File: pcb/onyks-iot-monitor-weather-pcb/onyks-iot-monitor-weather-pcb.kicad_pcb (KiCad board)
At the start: 2 copper layers, 100 x 82 mm, 32 parts, among them J1 53398-0371, J10 Conn_01x02_Pin, J11 Conn_01x06_Pin, J12 Conn_02x05_Odd_Even, J13 Conn_01x02_Pin, J2 53398-0371, J3 53048-0810, J4 53398-0371, J5 53398-0371, J6 53398-0371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

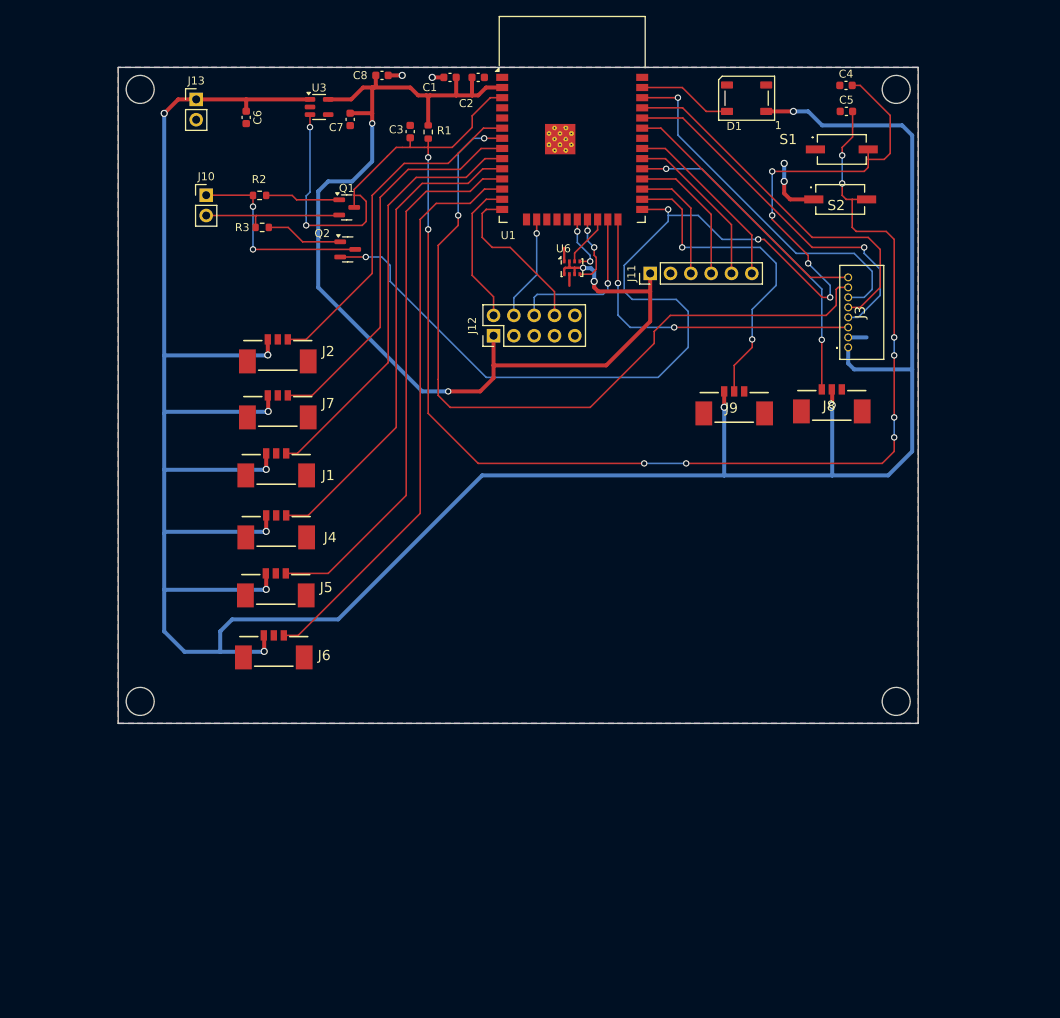
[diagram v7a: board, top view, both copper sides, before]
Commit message: Changed c1 c2 positions
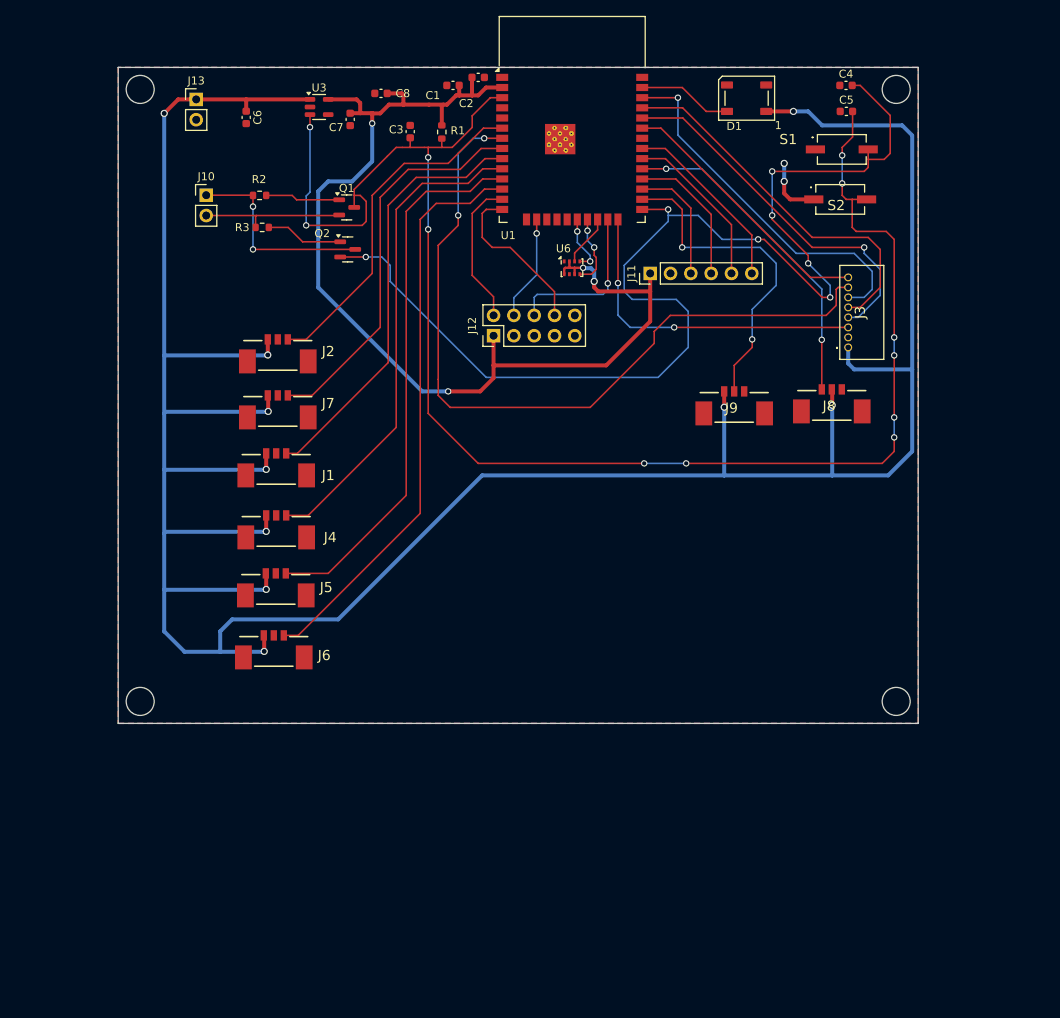
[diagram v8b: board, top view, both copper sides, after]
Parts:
- moved C8 2.25 mm to (125.6, 43.0), turned to 0 degrees
- moved R1 1.70 mm to (133.2, 47.8)
- moved C1 1.07 mm to (134.6, 42.0)
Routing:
- net GND: track 16.4 -> 7.77 mm, vias 4 -> 2
- net /3V3: track 141.7 -> 138.0 mm
